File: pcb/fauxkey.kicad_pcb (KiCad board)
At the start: 2 copper layers, 58.5 x 26.3 mm, 0 parts

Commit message: Design PCB v0.1
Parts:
- added C1: 10nF, Capacitor_SMD:C_0603_1608Metric, F.Cu at (120.0, 87.0)
- added C2: 10nF, Capacitor_SMD:C_0603_1608Metric, F.Cu at (126.5, 87.0)
- added J1: Conn_ARM_SWD_TagConnect_TC2030-NL, Connector:Tag-Connect_TC2030-IDC-NL_2x03_P1.27mm_Vertical, F.Cu at (169.6, 95.0)
- added J2: USB_C_Receptacle_USB2.0, Connector_USB:USB_C_Receptacle_GCT_USB4105-xx-A_16P_TopMnt_Horizontal, F.Cu at (120.2, 95.0)
- added J3: Conn_01x02, Connector_PinHeader_1.00mm:PinHeader_1x02_P1.00mm_Vertical, F.Cu at (126.1, 83.0)
- added R1: 5.1k, Resistor_SMD:R_0603_1608Metric, F.Cu at (119.9, 102.6)
- added R2: 5.1k, Resistor_SMD:R_0603_1608Metric, F.Cu at (123.1, 102.6)
- added R3: 800k, Resistor_SMD:R_0603_1608Metric, F.Cu at (155.5, 85.0)
- added R4: 2M, Resistor_SMD:R_0603_1608Metric, F.Cu at (160.0, 85.0)
- added R5: 2k, Resistor_SMD:R_0603_1608Metric, F.Cu at (166.9, 104.1)
- added U1: E73-2G4M08S1C, E73-2G4M08S1C:E73-2G4M08S1C, F.Cu at (158.0, 95.2)
- added U2: LTC4054ES5-4.2, Package_TO_SOT_SMD:TSOT-23-5, F.Cu at (123.2, 87.0)
- added Y1: 32.768 kHz, Crystal:Crystal_SMD_3225-4Pin_3.2x2.5mm, F.Cu at (150.1, 84.5)
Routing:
- net GND: track 0.00 -> 172.0 mm, vias 0 -> 8
- net /Power/USB_VBUS: track 0.00 -> 81.4 mm
- net /Power/PROG: track 0.00 -> 71.0 mm, vias 0 -> 2
- net /Power/USB_D+: track 0.00 -> 53.1 mm
- net /Power/USB_D-: track 0.00 -> 52.4 mm
- net /Power/VCC: track 0.00 -> 50.1 mm, vias 0 -> 8
- net Net-(J1-~{RESET}): track 0.00 -> 41.6 mm, vias 0 -> 2
- net unconnected-(U1-P0.26-Pad12): track 0.00 -> 27.2 mm, vias 0 -> 2
- net Net-(J1-SWCLK): track 0.00 -> 22.4 mm, vias 0 -> 2
- net Net-(J1-SWDIO): track 0.00 -> 22.4 mm, vias 0 -> 2
- net Net-(U1-P0.00/XL1): track 0.00 -> 21.8 mm
- net Net-(U1-P0.01/XL2): track 0.00 -> 14.9 mm
- net Net-(J2-CC2): track 0.00 -> 11.0 mm
- net Net-(J2-CC1): track 0.00 -> 10.8 mm, vias 0 -> 2
- net /Power/VCC_DIV: track 0.00 -> 6.31 mm
- added copper zone on B.Cu, net /Power/VCC
- added copper zone on F.Cu, net GND
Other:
- outline, holes or cut-outs redrawn
- board text added: "JLCJLCJLCJLC"
- board text added: "fauxkey v0.1"

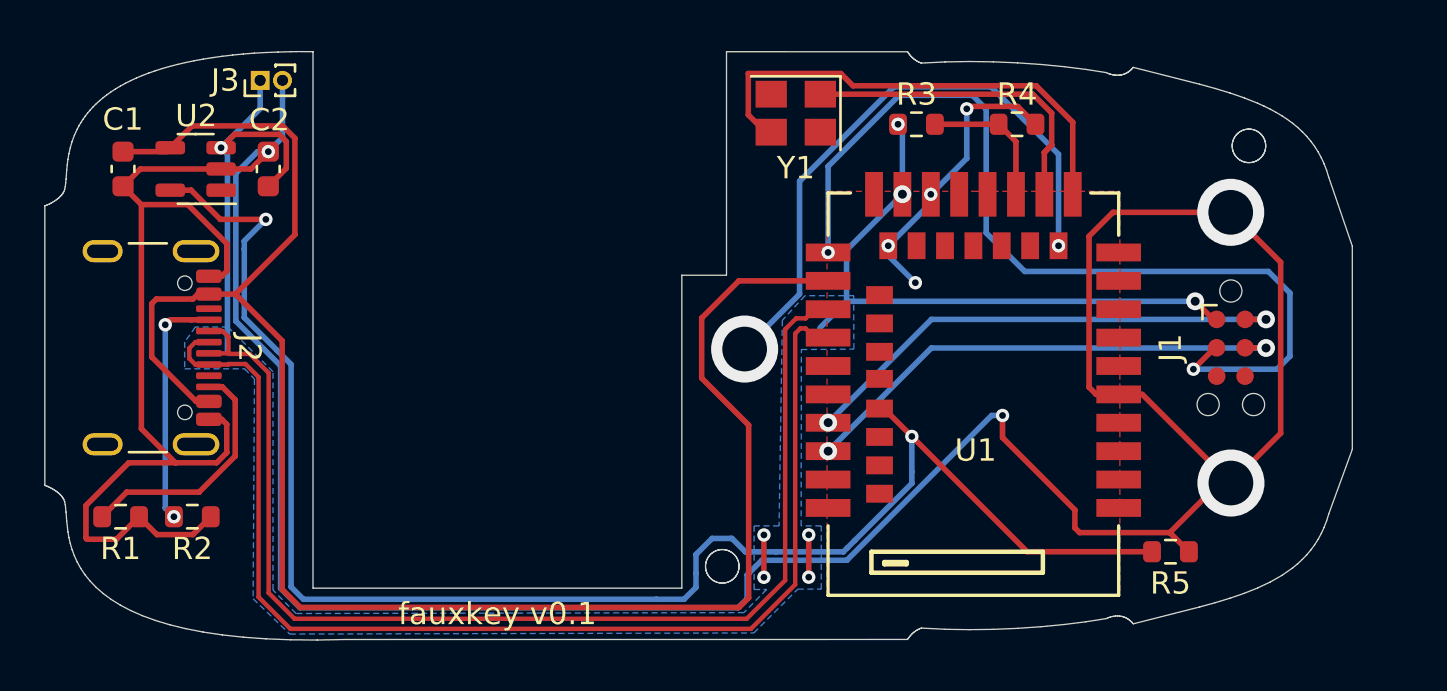
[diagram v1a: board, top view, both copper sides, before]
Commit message: PCB v0.2
Changes:
  - Fix the crystal footprint to be for 32.768 kHz crystals, not MHz
  - Add load capacitors to crystal
  - Make the footprint for the battery wires larger
  - Mark the positive pin on the battery pins
  - Remove extraneous footprint labels
  - Fix island in module ground plane
  - Resize pad connection holes to support Mill Max 0850
  - Resize mounting holes to match the actual PCB
  - Connect both sides of the cutout for rigidity
  - Allow mounting the USB-C connector on either side of the PCB
  - Replace Tag-Connect footprint with the cable I actually have
  - Move all used pins to the outside of the module
  - Break out a pair of unused pins for UART or whatever
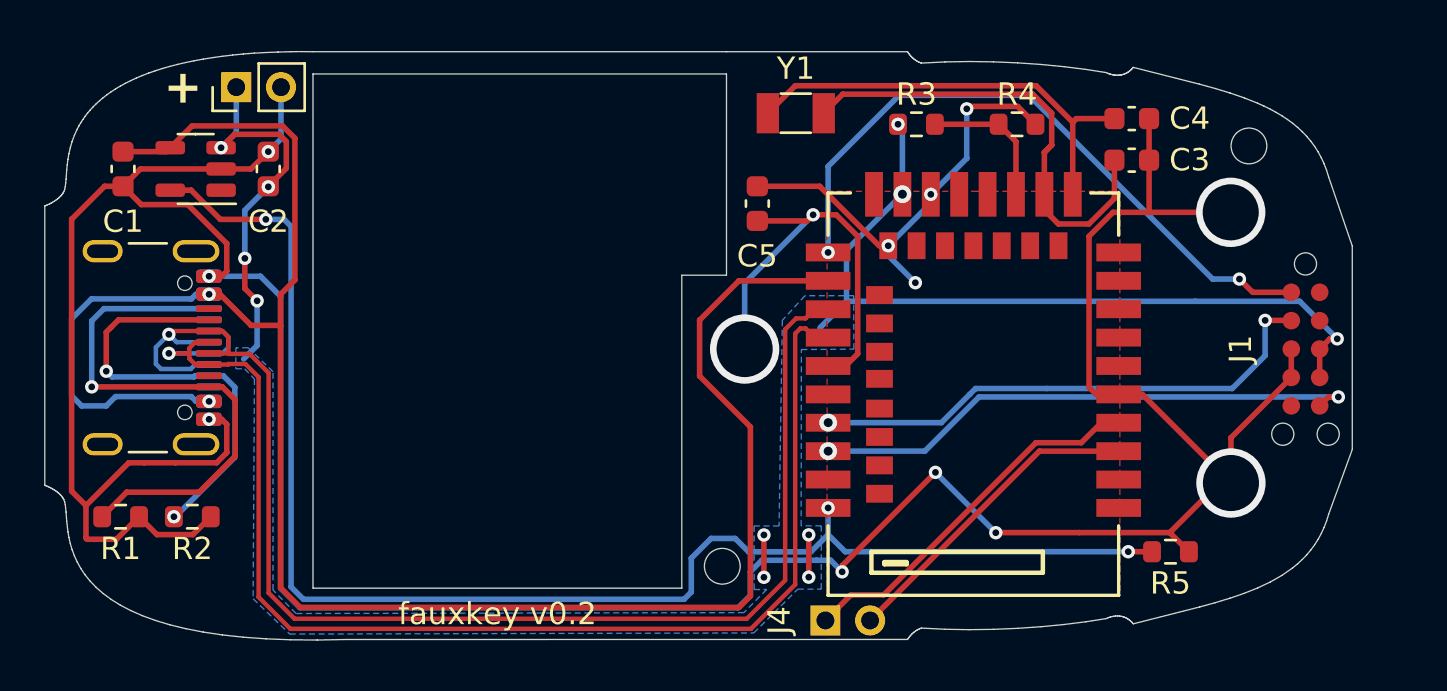
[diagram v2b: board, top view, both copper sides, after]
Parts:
- added C3: 12pF, Capacitor_SMD:C_0603_1608Metric, F.Cu at (165.1, 86.6)
- added C4: 12pF, Capacitor_SMD:C_0603_1608Metric, F.Cu at (165.1, 84.7)
- added C5: 10uF, Capacitor_SMD:C_0603_1608Metric, F.Cu at (148.4, 88.5)
- added J4: Conn_01x02, fauxkey:PinHeader_1x02_P2.00mm_Vertical_NoSilkscreen, F.Cu at (151.4, 107.2)
- C1, C2: value 10nF -> 10uF
- J1: value Conn_ARM_SWD_TagConnect_TC2030-NL -> Conn_ARM_JTAG_SWD_10; footprint Connector:Tag-Connect_TC2030-IDC-NL_2x03_P1.27mm_Vertical -> fauxkey:Tag-Connect_TC2050-IDC-NL_2x05_P1.27mm_Vertical_NoSilkscreen
- J2: footprint Connector_USB:USB_C_Receptacle_GCT_USB4105-xx-A_16P_TopMnt_Horizontal -> fauxkey:USB_C_Receptacle_GCT_USB4105-xx-A_16P_TopMnt_Horizontal_BothSides
- J3: footprint Connector_PinHeader_1.00mm:PinHeader_1x02_P1.00mm_Vertical -> Connector_PinHeader_2.00mm:PinHeader_1x02_P2.00mm_Vertical
- Y1: footprint Crystal:Crystal_SMD_3225-4Pin_3.2x2.5mm -> Crystal:Crystal_SMD_3215-2Pin_3.2x1.5mm
- moved J1 3.34 mm to (172.9, 95.1)
- moved J3 1.11 mm to (125.1, 83.3)
- turned Y1 to 0 degrees
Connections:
- J1 pad 1: /Power/VCC -> Net-(J1-RST)
- J1 pad 3: Net-(J1-~{RESET}) -> GND
- J1 pad 4: Net-(J1-SWCLK) -> GND
- J1 pad 6: unconnected-(J1-SWO-Pad6) -> Net-(J1-SWDCLK)
- U1 pad 26: Net-(J1-~{RESET}) -> Net-(J1-RST)
- U1 pad 3: unconnected-(U1-P0.03/AIN1*-Pad3) -> Net-(J4-Pin_2)
- U1 pad 33: unconnected-(U1-P0.13-Pad33) -> /KEY_PWR
- U1 pad 36: /Power/PROG -> unconnected-(U1-P1.00-Pad36)
- U1 pad 39: Net-(J1-SWCLK) -> Net-(J1-SWDCLK)
- U1 pad 4: unconnected-(U1-P0.28/AIN4*-Pad4) -> Net-(J4-Pin_1)
- U1 pad 43: unconnected-(U1-P0.10/NFC2*-Pad43) -> /Power/PROG
- Y1 pad 2: unconnected-(Y1-Pad2) -> Net-(U1-P0.00/XL1)
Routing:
- net Net-(J1-~{RESET}): track 41.6 -> 0.00 mm, vias 2 -> 0
- net Net-(J1-RST): track 0.00 -> 29.5 mm, vias 0 -> 2
- net unconnected-(U1-P0.26-Pad12): track 27.2 -> 0.00 mm, vias 2 -> 0
- net Net-(J1-SWDCLK): track 0.00 -> 24.8 mm, vias 0 -> 2
- net Net-(J1-SWCLK): track 22.4 -> 0.00 mm, vias 2 -> 0
- net /KEY_PWR: track 0.00 -> 19.1 mm, vias 0 -> 2
- net Net-(J4-Pin_1): track 0.00 -> 16.8 mm
- net Net-(J4-Pin_2): track 0.00 -> 14.3 mm
- net Net-(J2-CC2): track 11.0 -> 24.7 mm, vias 0 -> 1
- net /Power/USB_VBUS: track 81.4 -> 90.6 mm, vias 0 -> 2
- net Net-(J2-CC1): track 10.8 -> 19.6 mm
- net /Power/USB_D-: track 52.4 -> 60.3 mm, vias 0 -> 1
- net /Power/VCC: track 50.1 -> 56.7 mm, vias 8 -> 11
- net Net-(U1-P0.01/XL2): track 14.9 -> 21.4 mm
- net /Power/PROG: track 71.0 -> 65.1 mm, vias 2 -> 3
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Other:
- outline, holes or cut-outs redrawn
- board text added: "+"
- board text added: "fauxkey v0.2"
- board text removed: "fauxkey v0.1"
